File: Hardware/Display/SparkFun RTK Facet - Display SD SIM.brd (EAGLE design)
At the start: 50 x 23 mm, 42 parts, among them J1 FPC_12_0.5MM_BACKFLIP, J16 microSD, J3 FPC_12_0.5MM_BACKFLIP, U13 LIS2DH12

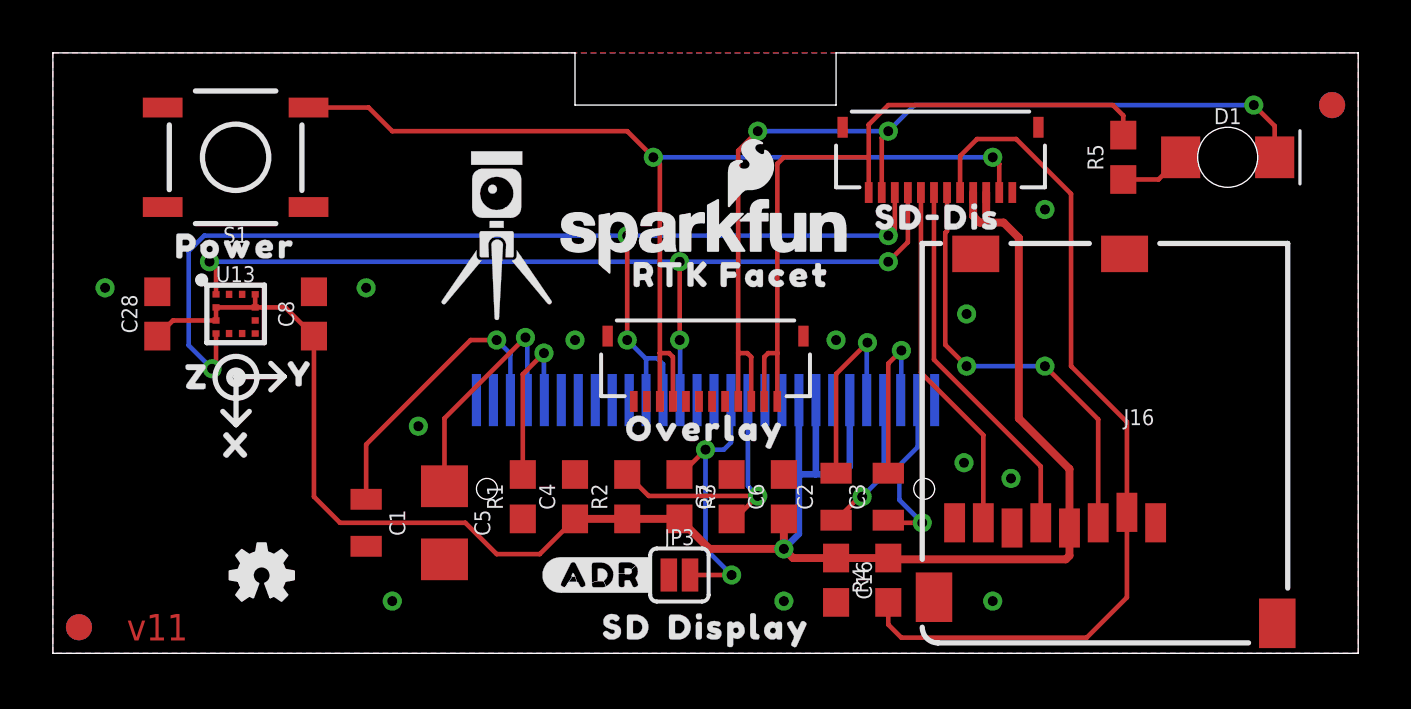
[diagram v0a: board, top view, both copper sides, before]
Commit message: Adding production panels.
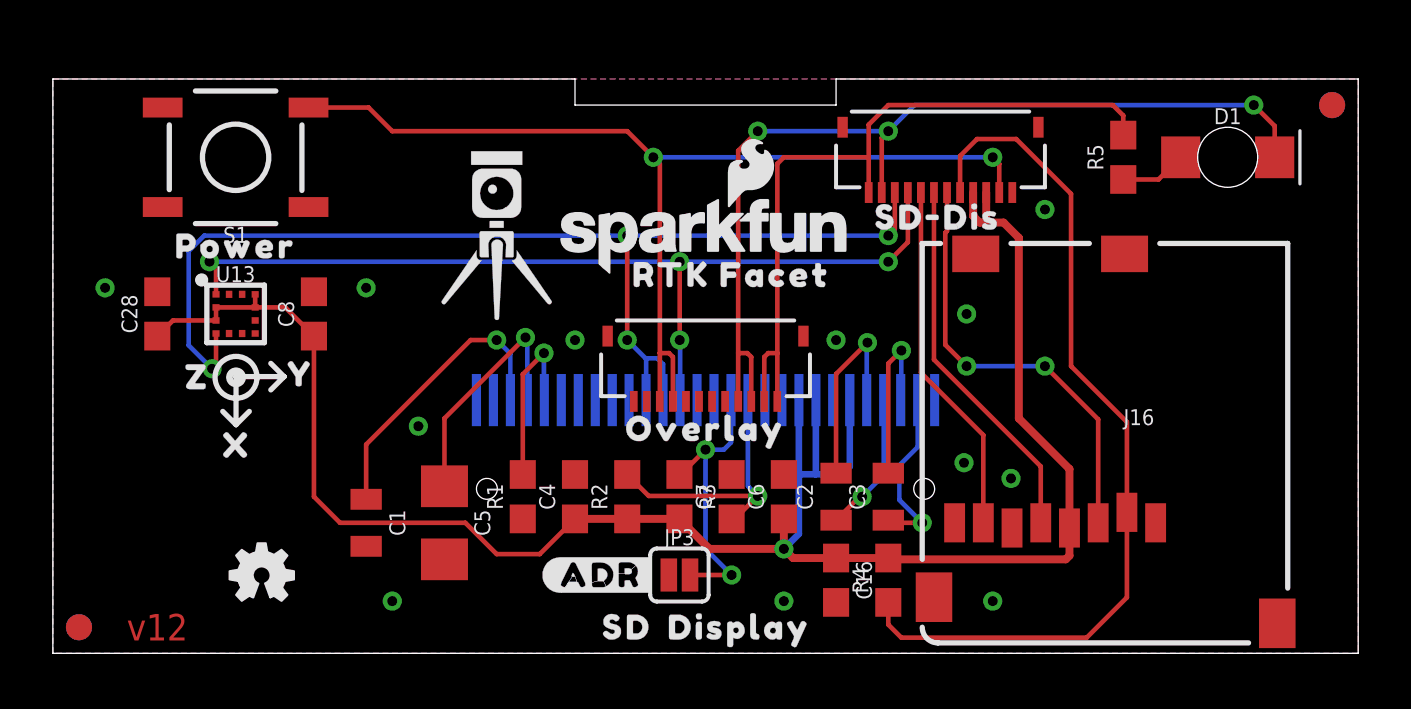
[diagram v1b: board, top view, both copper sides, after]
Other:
- board size 50 x 23 mm -> 50 x 22 mm
- board text added: "v12"
- board text removed: "v11"
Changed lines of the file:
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@@
 <layer number="23" name="tOrigins" color="15" fill="1" visible="yes" active="yes"/>
 <layer number="24" name="bOrigins" color="15" fill="1" visible="yes" active="yes"/>
-<layer number="25" name="tNames" color="7" fill="1" visible="no" active="yes"/>
-<layer number="26" name="bNames" color="7" fill="1" visible="no" active="yes"/>
-<layer number="27" name="tValues" color="7" fill="1" visible="no" active="yes"/>
-<layer number="28" name="bValues" color="7" fill="1" visible="no" active="yes"/>
-<layer number="29" name="tStop" color="7" fill="3" visible="no" active="yes"/>
-<layer number="30" name="bStop" color="7" fill="6" visible="no" active="yes"/>
-<layer number="31" name="tCream" color="7" fill="4" visible="no" active="yes"/>
-<layer number="32" name="bCream" color="7" fill="5" visible="no" active="yes"/>
-<layer number="33" name="tFinish" color="6" fill="3" visible="no" active="yes"/>
-<layer number="34" name="bFinish" color="6" fill="6" visible="no" active="yes"/>
-<layer number="35" name="tGlue" color="7" fill="4" visible="no" active="yes"/>
-<layer number="36" name="bGlue" color="7" fill="5" visible="no" active="yes"/>
-<layer number="37" name="tTest" color="7" fill="1" visible="no" active="yes"/>
-<layer number="38" name="bTest" color="7" fill="1" visible="no" active="yes"/>
-<layer number="39" name="tKeepout" color="4" fill="11" visible="no" active="yes"/>
-<layer number="40" name="bKeepout" color="1" fill="11" visible="no" active="yes"/>
+<layer number="25" name="tNames" color="7" fill="1" visible="yes" active="yes"/>
+<layer number="26" name="bNames" color="7" fill="1" visible="yes" active="yes"/>
+<layer number="27" name="tValues" color="7" fill="1" visible="yes" active="yes"/>
+<layer number="28" name="bValues" color="7" fill="1" visible="yes" active="yes"/>
+<layer number="29" name="tStop" color="7" fill="3" visible="yes" active="yes"/>
+<layer number="30" name="bStop" color="7" fill="6" visible="yes" active="yes"/>
+<layer number="31" name="tCream" color="7" fill="4" visible="yes" active="yes"/>
+<layer number="32" name="bCream" color="7" fill="5" visible="yes" active="yes"/>
+<layer number="33" name="tFinish" color="6" fill="3" visible="yes" active="yes"/>
+<layer number="34" name="bFinish" color="6" fill="6" visible="yes" active="yes"/>
+<layer number="35" name="tGlue" color="7" fill="4" visible="yes" active="yes"/>
+<layer number="36" name="bGlue" color="7" fill="5" visible="yes" active="yes"/>
+<layer number="37" name="tTest" color="7" fill="1" visible="yes" active="yes"/>
+<layer number="38" name="bTest" color="7" fill="1" visible="yes" active="yes"/>
+<layer number="39" name="tKeepout" color="4" fill="11" visible="yes" active="yes"/>
+<layer number="40" name="bKeepout" color="1" fill="11" visible="yes" active="yes"/>
 <layer number="41" name="tRestrict" color="4" fill="10" visible="yes" active="yes"/>
-<layer number="42" name="bRestrict" color="1" fill="10" visible="no" active="yes"/>
-<layer number="43" name="vRestrict" color="2" fill="10" visible="no" active="yes"/>
-<layer number="44" name="Drills" color="7" fill="1" visible="no" active="yes"/>
+<layer number="42" name="bRestrict" color="1" fill="10" visible="yes" active="yes"/>
+<layer number="43" name="vRestrict" color="2" fill="10" visible="yes" active="yes"/>
+<layer number="44" name="Drills" color="7" fill="1" visible="yes" active="yes"/>
 <layer number="45" name="Holes" color="7" fill="1" visible="yes" active="yes"/>
-<layer number="46" name="Milling" color="3" fill="1" visible="no" active="yes"/>
-<layer number="47" name="Measures" color="7" fill="1" visible="no" active="yes"/>
-<layer number="48" name="Document" color="7" fill="1" visible="no" active="yes"/>
-<layer number="49" name="Reference" color="7" fill="1" visible="no" active="yes"/>
-<layer number="50" name="dxf" color="7" fill="1" visible="no" active="yes"/>
+<layer number="46" name="Milling" color="3" fill="1" visible="yes" active="yes"/>
+<layer number="47" name="Measures" color="7" fill="1" visible="yes" active="yes"/>
+<layer number="48" name="Document" color="7" fill="1" visible="yes" active="yes"/>
+<layer number="49" name="Reference" color="7" fill="1" visible="yes" active="yes"/>
+<layer number="50" name="dxf" color="7" fill="1" visible="yes" active="yes"/>
 <layer number="51" name="tDocu" color="6" fill="1" visible="yes" active="yes"/>
-<layer number="52" name="bDocu" color="7" fill="1" visible="no" active="yes"/>
+<layer number="52" name="bDocu" color="7" fill="1" visible="yes" active="yes"/>
 <layer number="91" name="Nets" color="2" fill="1" visible="no" active="no"/>
 <layer number="92" name="Busses" color="1" fill="1" visible="no" active="no"/>
@@
 <board>
 <plain>
-<text x="4" y="1" size="1.016" layer="1" font="vector" ratio="20" rot="R180" align="center">v11</text>
-<wire x1="0" y1="0" x2="0" y2="23" width="0.05" layer="20"/>
-<wire x1="50" y1="23" x2="50" y2="0" width="0.05" layer="20"/>
+<text x="4" y="1" size="1.016" layer="1" font="vector" ratio="20" rot="R180" align="center">v12</text>
+<wire x1="0" y1="0" x2="0" y2="22" width="0.05" layer="20"/>
+<wire x1="50" y1="22" x2="50" y2="0" width="0.05" layer="20"/>
 <wire x1="50" y1="0" x2="0" y2="0" width="0.05" layer="20"/>
 <rectangle x1="48" y1="0" x2="50" y2="22" layer="40" rot="R180"/>
@@
 <text x="59" y="21" size="0.5" layer="51" font="vector" ratio="15" align="center">FPC stiffener is 3mm</text>
 <dimension x1="51" y1="22" x2="51" y2="19" x3="53" y3="20.5" textsize="0.5" textratio="15" layer="51" width="0.05"/>
-<wire x1="20" y1="23" x2="0" y2="23" width="0.05" layer="20"/>
-<wire x1="30" y1="23" x2="50" y2="23" width="0.05" layer="20"/>
-<wire x1="30" y1="21" x2="30" y2="23" width="0.05" layer="20"/>
-<wire x1="20" y1="21" x2="20" y2="23" width="0.05" layer="20"/>
+<wire x1="20" y1="22" x2="0" y2="22" width="0.05" layer="20"/>
+<wire x1="30" y1="22" x2="50" y2="22" width="0.05" layer="20"/>
+<wire x1="30" y1="21" x2="30" y2="22" width="0.05" layer="20"/>
+<wire x1="20" y1="21" x2="20" y2="22" width="0.05" layer="20"/>
 <wire x1="30" y1="21" x2="20" y2="21" width="0.05" layer="20"/>
 <wire x1="7.016" y1="10.698" x2="7.016" y2="8.758" width="0.2032" layer="21"/>
@@
 <wire x1="8.856" y1="10.598" x2="8.348" y2="10.09" width="0.2032" layer="21"/>
 <wire x1="8.856" y1="10.598" x2="8.348" y2="11.106" width="0.2032" layer="21"/>
-<dimension x1="0" y1="23" x2="0" y2="0" x3="-4" y3="11.5" textsize="1" layer="47" width="0.1"/>
+<dimension x1="0" y1="22" x2="0" y2="0" x3="-4" y3="11" textsize="1" layer="47" width="0.1"/>
 <dimension x1="0" y1="22" x2="50" y2="22" x3="25" y3="26" textsize="1" layer="47" width="0.1"/>
 <rectangle x1="22.4" y1="9.5" x2="22.6" y2="9.8" layer="41"/>
+<dimension x1="45" y1="19" x2="45" y2="22" x3="52" y3="20.5" textsize="1" layer="47" width="0.1"/>
+<dimension x1="45" y1="19" x2="50" y2="19" x3="47.5" y3="23" textsize="1" layer="47" width="0.1"/>
 </plain>
 <attributes>
@@
 <polygon width="0.1524" layer="1" isolate="0.1524">
 <vertex x="0" y="0"/>
-<vertex x="0" y="23"/>
-<vertex x="50" y="23"/>
+<vertex x="0" y="22"/>
+<vertex x="50" y="22"/>
 <vertex x="50" y="0"/>
 </polygon>
 <polygon width="0.1524" layer="16" isolate="0.1524">
 <vertex x="0" y="0"/>
-<vertex x="0" y="23"/>
-<vertex x="50" y="23"/>
+<vertex x="0" y="22"/>
+<vertex x="50" y="22"/>
 <vertex x="50" y="0"/>
 </polygon>

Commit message: Change to external pins SD socket on display board.
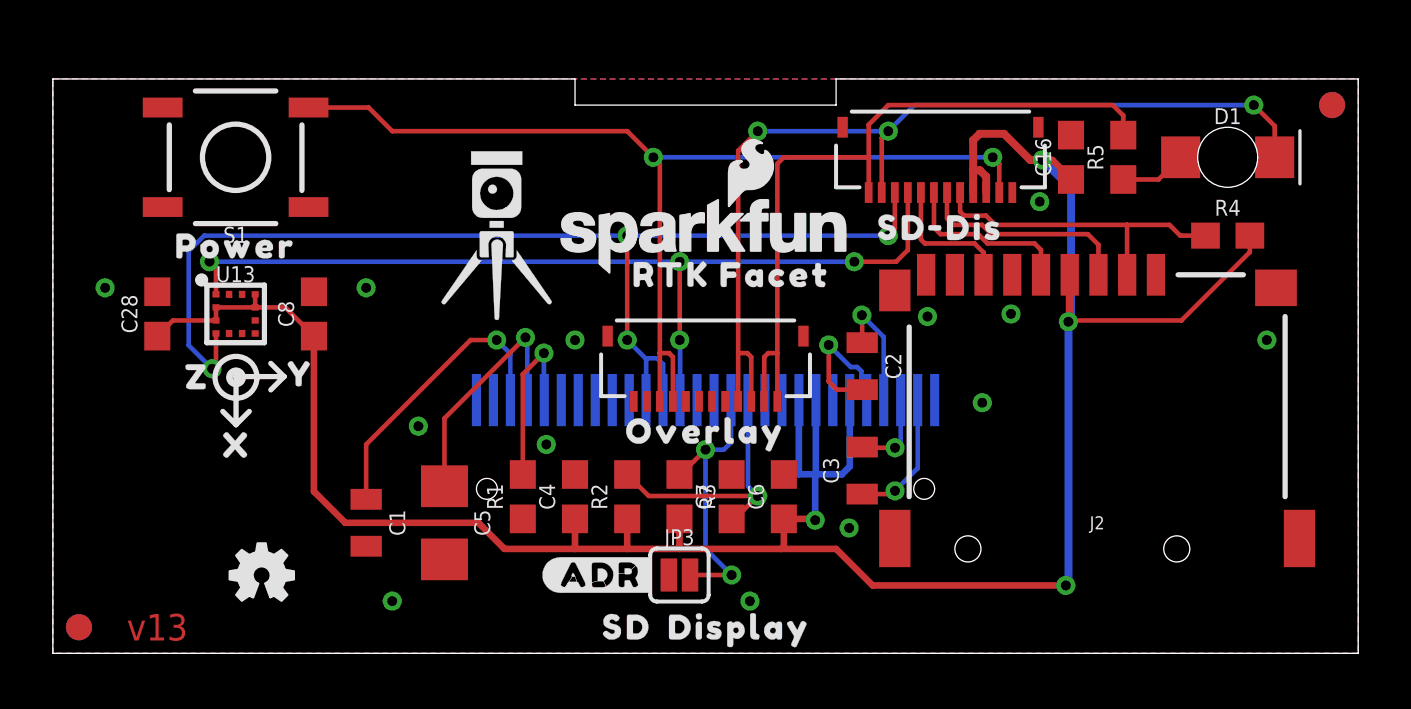
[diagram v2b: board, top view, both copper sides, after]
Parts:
- removed J16: microSD, SparkFun-Connectors:MICRO-SD-SOCKET
- added J2: MICRO-SD-PUSH-PUSH-EXT-PIN, SparkFun-Connectors:MICROSD-EXTERNALPIN
- S1: value (none) -> MOMENTARY-SWITCH-SPST-SMD-5.2MM-TALL
- moved C16 18.5 mm to (39.0, 19.0), turned to 90 degrees
- moved R4 18.5 mm to (45.0, 16.0), turned to 0 degrees
- moved C2 5.10 mm to (31.0, 11.0), turned to 270 degrees
- moved C3 1.41 mm to (31.0, 7.00)
- moved U$1 0.41 mm to (34.0, 16.3)
- moved U$2 0.10 mm to (25.0, 8.50)
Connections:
- net 3.3V: now also J2.4; no longer J16.VCC
- net GND: now also J2.10, J2.11, J2.12, J2.13, J2.6, J2.9; no longer J16.CD1, J16.GND, J16.GND1, J16.GND3
- net SD_!CS!: now also J2.2; no longer J16.CS/DAT3
- net SD_CIPO: now also J2.7; no longer J16.DO/DAT0
- net SD_COPI: now also J2.3; no longer J16.DI/CMD
- net SD_SCK: now also J2.5; no longer J16.SCLK
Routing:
- net SD_!CS!: track 34.0 -> 12.4 mm
- net 3.3V: track 76.6 -> 97.0 mm, vias 1 -> 4
- net SD_COPI: track 16.9 -> 8.36 mm, vias 2 -> 0
- net SD_CIPO: track 13.6 -> 5.26 mm
- net SD_SCK: track 14.3 -> 6.75 mm
- net C2N: track 6.82 -> 3.18 mm
- net N$2: track 7.71 -> 5.67 mm
- net N$1: track 6.69 -> 5.15 mm
- net C1P: track 5.41 -> 4.66 mm
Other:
- board text added: "v13"
- board text removed: "v12"

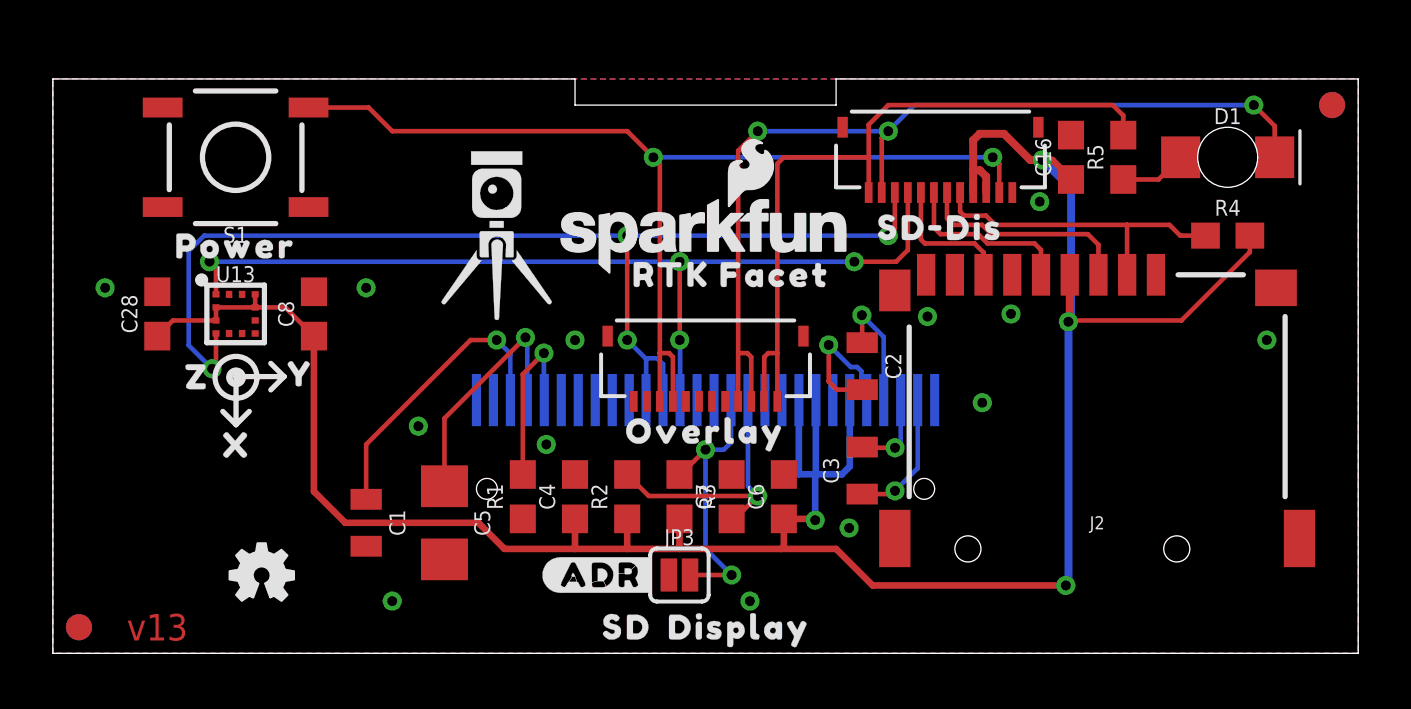
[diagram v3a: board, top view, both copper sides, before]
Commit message: Reduce Main, Connector, Display, and Cell board widths by 1mm to allow for v-score protrusion.
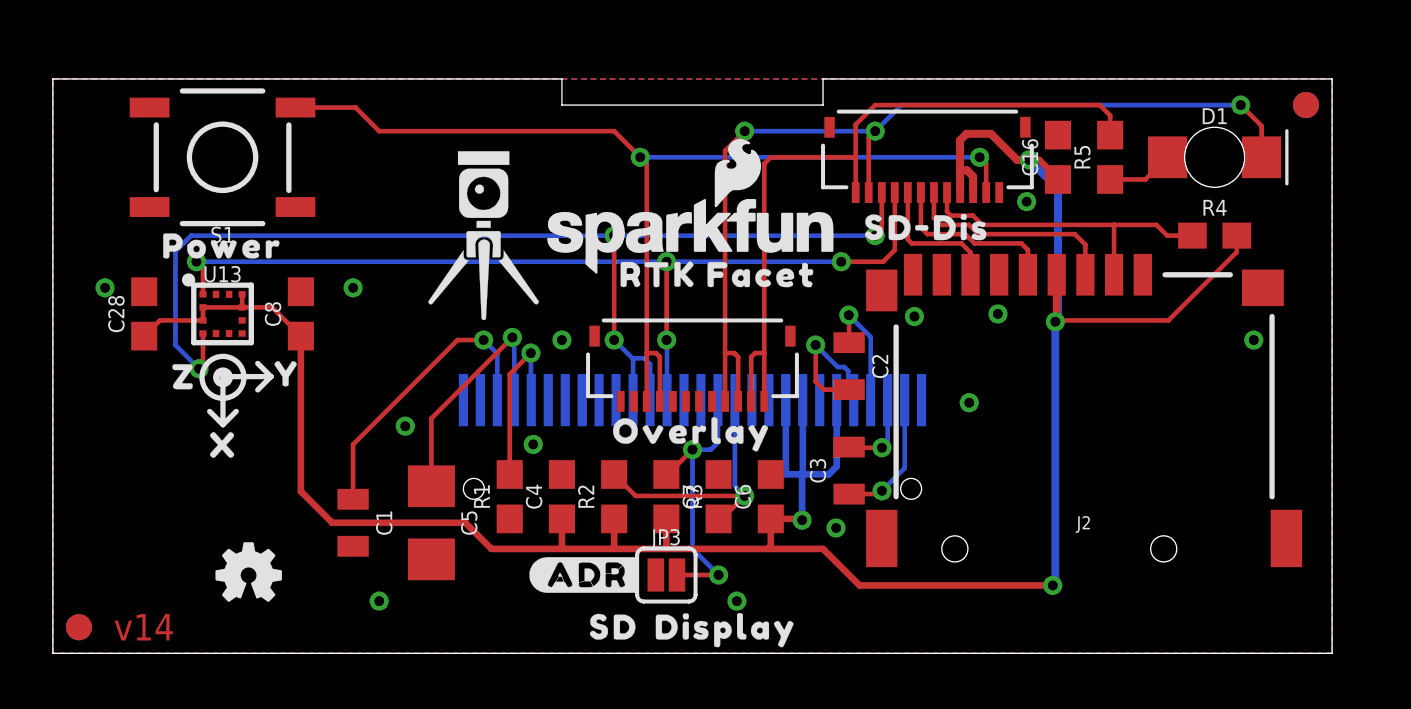
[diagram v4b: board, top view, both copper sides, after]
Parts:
- moved FID2 1.00 mm to (48.0, 21.0)
- moved FID3 1.00 mm to (48.0, 21.0)
- moved C1 0.50 mm to (11.5, 5.00)
- moved C16 0.50 mm to (38.5, 19.0)
- moved C2 0.50 mm to (30.5, 11.0)
- moved C28 0.50 mm to (3.50, 13.0)
- moved C3 0.50 mm to (30.5, 7.00)
- moved C4 0.50 mm to (19.5, 6.00)
- moved C5 0.50 mm to (14.5, 5.00)
- moved C6 0.50 mm to (27.5, 6.00)
- moved C7 0.50 mm to (25.5, 6.00)
- moved C8 0.50 mm to (9.50, 13.0)
- moved D1 0.50 mm to (44.5, 19.0)
- moved J1 0.50 mm to (33.5, 19.0)
- moved J2 0.50 mm to (39.5, 4.00)
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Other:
- board size 50 x 22 mm -> 49 x 22 mm
- board text added: "v14"
- board text removed: "v13"
